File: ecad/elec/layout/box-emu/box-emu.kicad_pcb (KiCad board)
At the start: 2 copper layers, 72.5 x 63.9 mm, 70 parts

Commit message: feat(ecad): Update ecad / atopile and improve workflow
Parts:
- removed DS1: , lib:SOD-323_L1.8-W1.3-LS2.5-RD
- removed R27: 62.5mW Thick Film Resistors 50V ±100ppm/℃ ±1% 249Ω 0402 Chi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, lib:R0402
- removed U10: , Connector_PinHeader_1.00mm:PinHeader_1x02_P1.00mm_Vertical
- removed U11: , lib:GAMEBOY_COLOR_DPAD_MEMBRANE
- removed U12, U13, U14, U15: , lib:GBC_DPAD_BUTTON
- removed U16, U19: , lib:GAMEBOY_COLOR_A_B_BUTTON_MEMBRANE
- removed U17, U18, U20, U21: , lib:GBC_A_B_BUTTON
- removed U22: , lib:GAMEBOY_COLOR_START_SELECT_MEMBRANE
- removed U23, U24: , lib:GBC_START_SELECT_BUTTON
- removed U25, U26: , lib:SW-SMD_TS24CA
- removed U27: , lib:BOX_EMU
- removed U28, U29: , lib:2X06_EDGE_REVERSED
- removed U30: , lib:2X02_EDGE_REVERSED
- removed U7: , lib:DFN-8_L2.0-W2.0-P0.50-BL-EP
- removed U8: , lib:SIM-SMD_C9900007362
- removed U9: , lib:VSSOP-10_L3.0-W3.0-P0.50-LS4.9-BL
- added C10: 22µF ±20%, Samsung_Electro_Mechanics_CL21A226MAQNNNE:C0805, F.Cu at (343.7, -323.6)
- added C11: 22µF ±20%, Samsung_Electro_Mechanics_CL21A226MAQNNNE:C0805, F.Cu at (343.7, -333.6)
- added C12: 100nF ±10%, Samsung_Electro_Mechanics_CL05B104KO5NNNC:C0402, F.Cu at (343.7, -363.6)
- added C13: 100nF ±10%, Samsung_Electro_Mechanics_CL05B104KO5NNNC:C0402, F.Cu at (343.7, -373.6)
- added CN1: , JST_Sales_America_S2B_PH_SM4_TB_LF__SN:CONN-SMD_P2.00_S2B-PH-SM4-TB-LF-SN, B.Cu at (32.4, 24.6)
- added CN2: , JST_Sales_America_SM04B_SRSS_TB_LF__SN:CONN-SMD_4P-P1.00_SM04B-SRSS-TB-LF-SN, F.Cu at (73.7, -33.6)
- added D1: , Guangdong_Hottech_1N5819WS:SOD-323_L1.8-W1.3-LS2.5-RD, F.Cu at (29.6, 17.7)
- added H1: , Ckmtw_B_2100S02P_A110:HDR-TH_2P-P2.54-V-M-1, F.Cu at (44.8, -31.2)
- added J2: , PMOD_2X06_EDGE:2X06_EDGE_REVERSED, F.Cu at (310.0, 0.00)
- added J3: , PMOD_2X06_EDGE:2X06_EDGE_REVERSED, F.Cu at (320.0, 0.00)
- added MECH1: , GBC_A_B_MEMBRANE:GAMEBOY_COLOR_A_B_BUTTON_MEMBRANE, F.Cu at (64.8, -4.19)
- added MECH2: , GBC_A_B_MEMBRANE:GAMEBOY_COLOR_A_B_BUTTON_MEMBRANE, F.Cu at (59.6, -19.4)
- added MECH3: , GBC_DPAD_MEMBRANE:GAMEBOY_COLOR_DPAD_MEMBRANE, F.Cu at (20.8, -11.8)
- added MECH4: , BOX_EMU_BASE_OUTLINE:BOX_EMU_BASE, F.Cu at (43.7, -33.6)
- added MECH5: , GBC_START_SELECT_MEMBRANE:GAMEBOY_COLOR_START_SELECT_MEMBRANE, F.Cu at (42.2, 10.4)
- added MECH6: , BOX_EMU_OUTLINE:BOX_EMU, F.Cu at (300.0, 0.00)
- added SW1: , GBC_A_B_BUTTON:GBC_A_B_BUTTON, F.Cu at (71.8, -6.60)
- added SW10: , GBC_START_SELECT_BUTTON:GBC_START_SELECT_BUTTON, F.Cu at (48.4, 10.4)
- added SW11: , SHOU_HAN_TS24CA:SW-SMD_2P-TS24CA, F.Cu at (21.9, 29.1)
- added SW12: , SHOU_HAN_TS24CA:SW-SMD_2P-TS24CA, F.Cu at (27.9, 30.0)
- added SW2: , GBC_A_B_BUTTON:GBC_A_B_BUTTON, F.Cu at (57.9, -1.63)
- added SW3: , GBC_A_B_BUTTON:GBC_A_B_BUTTON, F.Cu at (66.6, -21.9)
- added SW4: , GBC_A_B_BUTTON:GBC_A_B_BUTTON, F.Cu at (52.7, -17.0)
- added SW5: , GBC_DPAD_BUTTON:GBC_DPAD_BUTTON, F.Cu at (20.8, -3.81)
- added SW6: , GBC_DPAD_BUTTON:GBC_DPAD_BUTTON, F.Cu at (12.8, -11.7)
- added SW7: , GBC_DPAD_BUTTON:GBC_DPAD_BUTTON, F.Cu at (28.8, -11.7)
- added SW8: , GBC_DPAD_BUTTON:GBC_DPAD_BUTTON, F.Cu at (20.8, -19.7)
- added SW9: , GBC_START_SELECT_BUTTON:GBC_START_SELECT_BUTTON, F.Cu at (36.8, 10.4)
- added USB1: , Yuandi_TYPE_611_T3_W:USB-C-SMD_TYPE-611-T3-W, F.Cu at (42.5, 30.3)
- C1: value 16V 100nF X7R ±10% 0402 Multilayer Ceramic Capacitors MLCC - SMD/SMT ROHS -> 100nF ±10%; footprint lib:C0402 -> Samsung_Electro_Mechanics_CL05B104KO5NNNC:C0402
- C2: value 25V 10uF X5R ±10% 0805 Multilayer Ceramic Capacitors MLCC - SMD/SMT ROHS -> 1µF ±10%; footprint lib:C0805 -> Samsung_Electro_Mechanics_CL05A105KA5NQNC:C0402
- C3, C4, C5: value 25V 10uF X5R ±10% 0805 Multilayer Ceramic Capacitors MLCC - SMD/SMT ROHS -> 100nF ±10%; footprint lib:C0805 -> Samsung_Electro_Mechanics_CL05B104KO5NNNC:C0402
- C6: value 16V 100nF X7R ±10% 0402 Multilayer Ceramic Capacitors MLCC - SMD/SMT ROHS -> 4.7µF ±10%; footprint lib:C0402 -> Samsung_Electro_Mechanics_CL05A475KP5NRNC:C0402
- C7: value 10V 4.7uF X5R ±20% 0402 Multilayer Ceramic Capacitors MLCC - SMD/SMT ROHS -> 4.7µF ±10%; footprint lib:C0402 -> Samsung_Electro_Mechanics_CL05A475KP5NRNC:C0402
- C8: value 10V 4.7uF X5R ±20% 0402 Multilayer Ceramic Capacitors MLCC - SMD/SMT ROHS -> 10µF ±10%; footprint lib:C0402 -> Samsung_Electro_Mechanics_CL21A106KAYNNNE:C0805
- C9: value 16V 100nF X7R ±10% 0402 Multilayer Ceramic Capacitors MLCC - SMD/SMT ROHS -> 10µF ±10%; footprint lib:C0402 -> Samsung_Electro_Mechanics_CL21A106KAYNNNE:C0805
- J1: footprint lib:CONN-SMD_4P-P1.00_SM04B-SRSS-TB-LF-SN -> PWR_2X02_EDGE:2X02_EDGE_REVERSED
- L1: footprint lib:IND-SMD_L2.5-W2.0_WPN252012H -> Sunlord_WPN252012H1R5MT:IND-SMD_L2.5-W2.0_WPN252012H
- LED1: footprint lib:LED0805-R-RD -> Yongyu_Photoelectric_SZYY0805R:LED0805-R-RD
- R1, R2: value 62.5mW Thick Film Resistors 50V ±100ppm/℃ ±1% 4.7kΩ 0402 Chip Resistor - Surface Mount ROHS -> 1MΩ ±1%; footprint lib:R0402 -> UNI_ROYAL_0402WGF1004TCE:R0402
- R10: value 62.5mW Thick Film Resistors 50V ±100ppm/℃ ±1% 2kΩ 0402 Chip Resistor - Surface Mount ROHS -> 10kΩ ±1%; footprint lib:R0402 -> UNI_ROYAL_0402WGF1002TCE:R0402
- R11: value 62.5mW Thick Film Resistors 50V ±100ppm/℃ ±1% 2.55kΩ 0402 Chip Resistor - Surface Mount ROHS -> 10kΩ ±1%; footprint lib:R0402 -> UNI_ROYAL_0402WGF1002TCE:R0402
- R12, R13, R14, R15, R16, R18, R19, R20, R25, R3, R4, R5, R6: value 62.5mW Thick Film Resistors 50V ±100ppm/℃ ±1% 10kΩ 0402 Chip Resistor - Surface Mount ROHS -> 10kΩ ±1%; footprint lib:R0402 -> UNI_ROYAL_0402WGF1002TCE:R0402
- R17, R23, R24: value 62.5mW Thick Film Resistors 50V ±100ppm/℃ ±1% 10kΩ 0402 Chip Resistor - Surface Mount ROHS -> 5.1kΩ ±1%; footprint lib:R0402 -> UNI_ROYAL_0402WGF5101TCE:R0402
- R21: value 62.5mW Thick Film Resistors 50V ±100ppm/℃ ±1% 10kΩ 0402 Chip Resistor - Surface Mount ROHS -> 91kΩ ±1%; footprint lib:R0402 -> YAGEO_RC0402FR_0791KL:R0402
- R22: value 62.5mW Thick Film Resistors 50V ±100ppm/℃ ±1% 10kΩ 0402 Chip Resistor - Surface Mount ROHS -> 820kΩ ±1%; footprint lib:R0402 -> FOJAN_FRC0402F8203TS:R0402
- R26: value 62.5mW Thick Film Resistors 50V ±100ppm/℃ ±1% 255Ω 0402 Chip Resistor - Surface Mount ROHS -> 10kΩ ±1%; footprint lib:R0402 -> UNI_ROYAL_0402WGF1002TCE:R0402
- R7: value 62.5mW Thick Film Resistors ±100ppm/℃ ±1% 243kΩ 0402 Chip Resistor - Surface Mount ROHS -> 2kΩ ±1%; footprint lib:R0402 -> UNI_ROYAL_0402WGF2001TCE:R0402
- R8: value 62.5mW Thick Film Resistors 50V ±100ppm/℃ ±1% 27.4kΩ 0402 Chip Resistor - Surface Mount ROHS -> 10kΩ ±1%; footprint lib:R0402 -> UNI_ROYAL_0402WGF1002TCE:R0402
- R9: value 62.5mW Thick Film Resistors 50V ±100ppm/℃ ±1% 1MΩ 0402 Chip Resistor - Surface Mount ROHS -> 10kΩ ±1%; footprint lib:R0402 -> UNI_ROYAL_0402WGF1002TCE:R0402
- U1: footprint lib:BOX_EMU_BASE -> Texas_Instruments_DRV2605LDGSR:VSSOP-10_L3.0-W3.0-P0.50-LS4.9-BL
- U2: footprint lib:CONN-SMD_P2.00_S2B-PH-SM4-TB-LF-SN -> AWINIC_AW9523BTQR:VFQFPN-24_L4.0-W4.0-P0.50-BL-EP2.8; moved to F.Cu
- U3: footprint lib:USB-C-SMD_TYPE-611-T3-W -> Maxim_Integrated_MAX17048G_T10:TDFN-8_L2.0-W2.0-P0.50-BL-EP1.2
- U4: footprint lib:VFQFPN-24_L4.0-W4.0-P0.50-BL-EP2.8 -> Microchip_Tech_MCP73831T_2ACI_OT:SOT-23-5_L3.0-W1.7-P0.95-LS2.8-BL
- U5: footprint lib:VSON-14_L4.0-W3.0-P0.50-BL-EP_TI_DSJ -> Texas_Instruments_TPS63020DSJR:VSON-14_L4.0-W3.0-P0.50-BL-EP_TI_DSJ
- U6: footprint lib:SOT-23-5_L3.0-W1.7-P0.95-LS2.8-BL -> HOAUC_HYCW118_TF09_200B:SIM-SMD_C9900007362
- moved R25 582.5 mm to (343.7, -403.6), turned to 0 degrees
- moved R26 580.2 mm to (343.7, -413.6), turned to 0 degrees
- moved R24 572.8 mm to (343.7, -393.6), turned to 0 degrees
- moved R23 542.9 mm to (343.7, -383.6), turned to 0 degrees
- moved R22 511.4 mm to (343.7, -353.6)
- moved C9 494.4 mm to (343.7, -313.6), turned to 0 degrees
- moved C8 484.6 mm to (343.7, -303.6), turned to 0 degrees
- moved R21 469.5 mm to (343.7, -343.6), turned to 0 degrees
- moved C6 455.6 mm to (343.7, -273.6), turned to 0 degrees
- moved C7 448.0 mm to (343.7, -263.6), turned to 0 degrees
- moved C5 443.0 mm to (343.7, -253.6), turned to 0 degrees
- moved R18 402.5 mm to (343.7, -243.6), turned to 0 degrees
- moved C4 399.9 mm to (343.7, -203.6), turned to 0 degrees
- moved R17 390.8 mm to (343.7, -233.6), turned to 0 degrees
- moved R16 385.9 mm to (343.7, -223.6), turned to 0 degrees
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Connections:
- net l1 renamed 1
- net l2 renamed 2
- C1 pad 1: vcc_3v3 -> battery_measurement
- C1 pad 2: box-gnd -> gnd
- C2 pad 1: vbat -> hv
- C2 pad 2: box-gnd -> gnd
- C3 pad 1: vbat -> vcc_3v3
- C3 pad 2: box-gnd -> gnd
- C4 pad 1: vcc_5v -> vcc_3v3
- C4 pad 2: box-gnd -> gnd
- C5 pad 1: vcc_5v -> vbat
- C5 pad 2: box-gnd -> gnd
- C6 pad 1: vina -> vbat
- C6 pad 2: box-gnd -> gnd
- C7 pad 2: box-gnd -> gnd
- C8 pad 2: box-gnd -> gnd
- C9 pad 2: box-gnd -> gnd
- J1 pad 1: box-gnd -> vcc_5v
- J1 pad 2: vcc_3v3 -> gnd
- J1 pad 3: sda -> gnd
- J1 pad 4: scl -> vcc_5v
- LED1 pad 1: vbus -> pos
- LED1 pad 2: cathode -> STAT
- R1 pad 1: cc1 -> battery_measurement
- R1 pad 2: box-gnd -> gnd
- R10 pad 1: prog -> vcc_3v3
- R10 pad 2: box-gnd -> right
- R11 pad 1: cathode -> vcc_3v3
- R11 pad 2: box.mcp73831-gnd -> up
- R12 pad 1: p1_3 -> EN
- R13 pad 1: en -> vcc_3v3
- R13 pad 2: vcc_3v3 -> SCL
- R14 pad 2: up -> SDA
- R15 pad 2: down -> INTN
- R16 pad 2: left -> RSTN
- R17 pad 1: vcc_3v3 -> vbus
- R17 pad 2: right -> pos
- R18 pad 1: vcc_3v3 -> nALRT
- R18 pad 2: box.io-a -> vcc_3v3
- R19 pad 2: box.io-b -> select
- R2 pad 1: cc2 -> vbat
- R2 pad 2: box-gnd -> battery_measurement
- R20 pad 2: x -> start
- R21 pad 1: vcc_3v3 -> FB
- R21 pad 2: y -> gnd
- R22 pad 1: vcc_3v3 -> vcc_5v
- R22 pad 2: start -> FB
- R23 pad 1: vcc_3v3 -> A5
- R23 pad 2: select -> gnd
- R24 pad 1: vcc_3v3 -> B5
- R24 pad 2: vol_up -> gnd
- R26 pad 1: vbat -> vcc_3v3
- R26 pad 2: battery_measurement -> vol_up
- R3 pad 1: sda -> vcc_3v3
- R3 pad 2: vcc_3v3 -> line
- R4 pad 1: scl -> vcc_3v3
- R4 pad 2: vcc_3v3 -> buttons_abxy-b-line
- R5 pad 2: rstn -> x_y_btns-a-line
- R6 pad 2: intn -> x_y_btns-b-line
- R7 pad 1: vcc_5v -> PROG
- R7 pad 2: out -> gnd
- R8 pad 1: out -> vcc_3v3
- R8 pad 2: box-gnd -> down
- R9 pad 1: pg -> vcc_3v3
- R9 pad 2: box-gnd -> left
- U2 pad 1: vbat -> start
- U2 pad 2: box-gnd -> select
- U2 pad 3: box-gnd -> 3
- U2 pad 4: box-gnd -> nALRT
- U4 pad 1: start -> STAT
- U4 pad 2: select -> gnd
- U4 pad 3: p1_2 -> vbat
- U4 pad 4: p1_3 -> vbus
- U4 pad 5: up -> PROG
- U5 pad 1: vina -> vbat
- U5 pad 12: vina -> vbat
- U5 pad 13: box-gnd -> gnd
- U5 pad 14: pg -> PG
- U5 pad 15: box-gnd -> gnd
- U5 pad 2: box-gnd -> gnd
- U5 pad 3: out -> FB
- U6 pad 1: box.mcp73831-gnd -> box.uSD.card-1
- U6 pad 2: box-gnd -> cs-line
- U6 pad 3: vbat -> MOSI
- U6 pad 4: vbus -> vcc_3v3
- U6 pad 5: prog -> SCLK
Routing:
- net box-gnd: track 462.7 -> 0.00 mm, vias 16 -> 0
- net vcc_3v3: track 170.7 -> 0.00 mm, vias 18 -> 0
- net sda: track 151.2 -> 0.00 mm, vias 7 -> 0
- net scl: track 142.5 -> 0.00 mm, vias 4 -> 0
- net miso: track 134.2 -> 0.00 mm, vias 2 -> 0
- net battery_measurement: track 127.9 -> 0.00 mm, vias 2 -> 0
- net dm: track 86.8 -> 0.00 mm, vias 2 -> 0
- net dp: track 79.5 -> 0.00 mm, vias 2 -> 0
- net box.io-b: track 77.7 -> 0.00 mm
- net sck: track 72.4 -> 0.00 mm, vias 2 -> 0
- net mosi: track 71.1 -> 0.00 mm, vias 2 -> 0
- net cs: track 70.0 -> 0.00 mm, vias 2 -> 0
- net down: track 69.4 -> 0.00 mm, vias 2 -> 0
- net vbus: track 68.5 -> 0.00 mm, vias 4 -> 0
- net y: track 63.1 -> 0.00 mm
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- removed copper zone on F.Cu, net box-gnd
- removed copper zone on B.Cu, net vcc_3v3
- removed copper zone on B.Cu, net vcc_5v
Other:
- board text removed: "A"
- board text removed: "B"
- board text removed: "DOWN"
- board text removed: "LEFT"
- board text removed: "RIGHT"
- board text removed: "SELECT"
- board text removed: "START"
- board text removed: "UP"
- board text removed: "X"
- board text removed: "Y"

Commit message: improve workflow
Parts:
- J1: moved to B.Cu
- moved J1 311.7 mm to (21.4, -43.9)
- moved J2 275.9 mm to (36.7, -37.5)
- moved J3 263.2 mm to (59.5, -37.5)
- moved MECH6 259.5 mm to (43.8, -41.2)
- moved U6 11.4 mm to (56.9, 24.5), turned to 6 degrees
- moved USB1 1.54 mm to (42.5, 28.7)
- moved CN1 0.46 mm to (32.7, 25.0), turned to 0 degrees
- turned SW11 to 170 degrees
- turned SW12 to 174 degrees
- turned SW3 to 180 degrees
- turned SW4 to 180 degrees
- turned SW5 to 90 degrees
- turned SW7 to 180 degrees
- turned SW8 to 270 degrees

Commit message: improve placement of components and robustness of scripts
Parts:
- MECH1, MECH2: value (none) -> SILKSCREENGBC_A/B
- REF**: renamed from MECH6; value (none) -> BOX_EMU
- REF**: renamed from MECH4; value (none) -> BOX_EMU_BASE
- U$1: renamed from MECH3; value (none) -> SILKSCREENGBC_D-PAD
- U$2: renamed from MECH5; value (none) -> SILKSCREENGBC_START/SELECT
- moved R24 556.2 mm to (165.6, 133.3), turned to 180 degrees
- moved R26 552.5 mm to (164.1, 108.9), turned to 180 degrees
- moved R23 547.9 mm to (165.6, 134.6), turned to 180 degrees
- moved R25 542.0 mm to (164.1, 107.7), turned to 180 degrees
- moved C13 527.9 mm to (179.4, 128.1), turned to 180 degrees
- moved C12 526.1 mm to (162.2, 130.2)
- moved R22 520.1 mm to (147.9, 128.2), turned to 180 degrees
- moved R21 509.8 mm to (147.9, 127.0), turned to 180 degrees
- moved C11 495.7 mm to (152.7, 123.8), turned to 90 degrees
- moved C9 482.7 mm to (153.5, 130.0), turned to 180 degrees
- moved C8 472.2 mm to (143.4, 124.0), turned to 90 degrees
- moved C10 447.8 mm to (154.6, 82.3), turned to 90 degrees
- moved C6 447.8 mm to (137.4, 123.8), turned to 90 degrees
- moved C7 438.2 mm to (159.8, 134.1)
- moved C5 432.6 mm to (157.0, 136.6)
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- renumbered SW4 to U2, SW2 to U2, SW1 to U2, SW3 to U2, J3 to U2, J2 to U2, SW10 to U3, SW9 to U3, J1 to U4, SW8 to U5, SW6 to U5, SW7 to U5, SW5 to U5

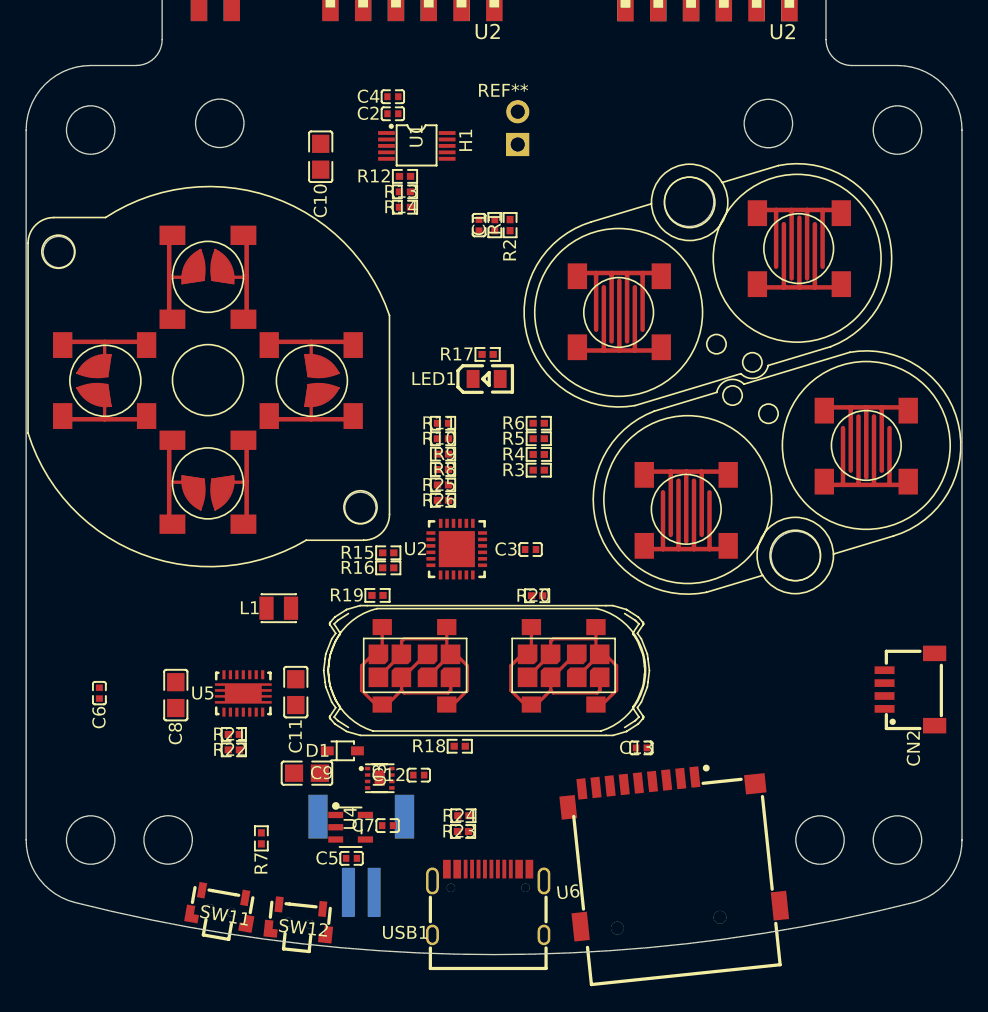
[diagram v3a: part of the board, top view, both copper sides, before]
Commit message: nudge layouts some
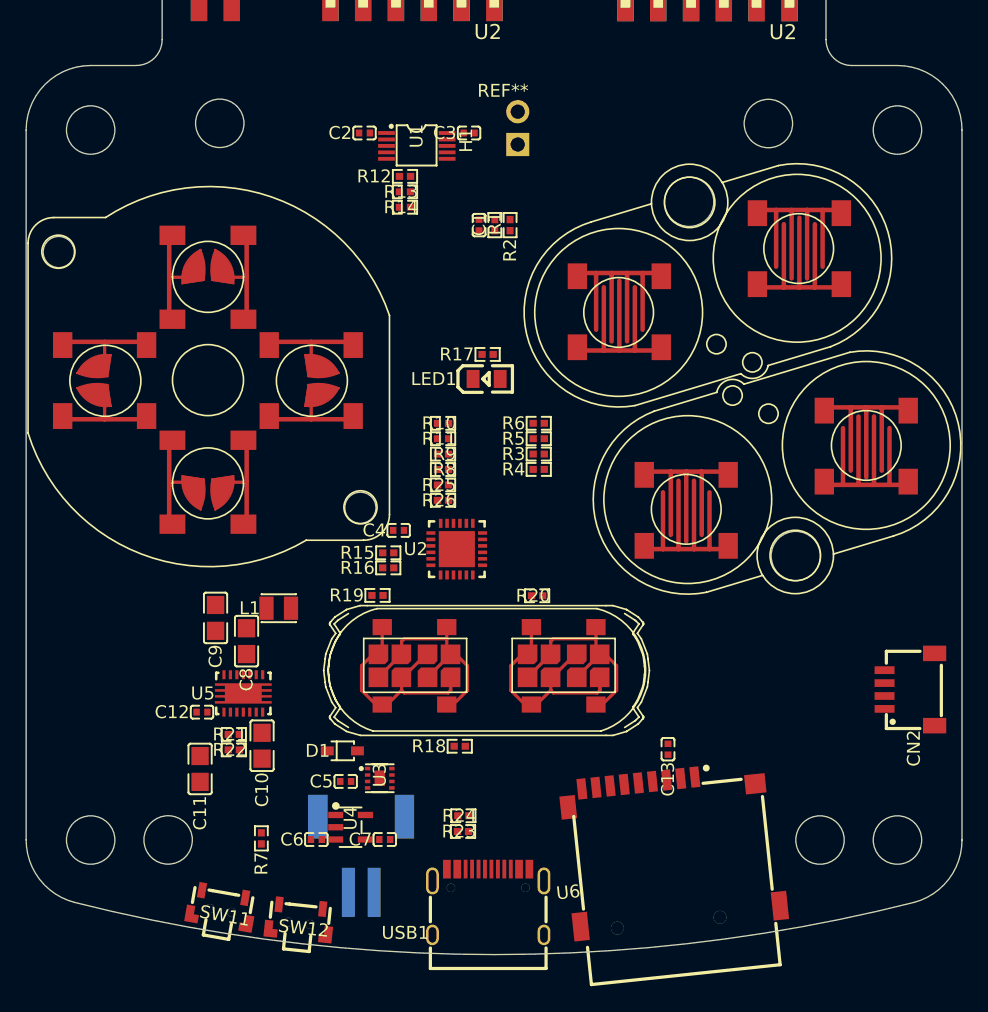
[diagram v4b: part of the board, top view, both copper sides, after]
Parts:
- moved C10 45.9 mm to (150.0, 127.9)
- moved C4 33.6 mm to (160.6, 111.2)
- moved C3 32.6 mm to (166.1, 80.4)
- moved C6 20.3 mm to (154.3, 135.2), turned to 0 degrees
- moved C12 17.5 mm to (145.4, 125.3)
- moved C9 14.0 mm to (146.4, 118.0), turned to 90 degrees
- moved C11 9.51 mm to (145.2, 129.7)
- moved C8 6.89 mm to (148.8, 119.8)
- moved C5 5.98 mm to (156.5, 130.7)
- moved C2 2.65 mm to (158.0, 80.4)
- moved C13 2.06 mm to (181.5, 128.2), turned to 90 degrees
- moved R3 1.25 mm to (171.5, 105.3)
- moved R11 1.19 mm to (164.1, 104.1)
- moved R10 1.19 mm to (164.1, 102.9)
- moved R4 1.16 mm to (171.5, 106.5)
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
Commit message: further layout changes
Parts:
- moved L1 6.66 mm to (152.2, 123.9), turned to 270 degrees
- moved C11 3.45 mm to (148.7, 129.8), turned to 180 degrees
- moved R22 2.15 mm to (146.0, 127.2)
- moved R21 2.14 mm to (146.0, 128.1), turned to 0 degrees
- moved C9 2.04 mm to (148.3, 118.9), turned to 180 degrees
- moved C10 1.36 mm to (148.7, 128.0), turned to 180 degrees
- moved C8 1.02 mm to (148.3, 120.7), turned to 180 degrees
- turned C12 to 180 degrees
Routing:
- net gnd: track 0.00 -> 21.5 mm
- net vcc_5v: track 0.00 -> 11.1 mm
- net vbat: track 0.00 -> 7.45 mm
- net FB: track 0.00 -> 5.29 mm
- net 2: track 0.00 -> 3.15 mm
- net 1: track 0.00 -> 3.15 mm

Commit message: fixing some issues
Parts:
- MECH1, MECH2: value SILKSCREENGBC_A/B -> (none)
- MECH3: renamed from REF**; value BOX_EMU_BASE -> (none)
- MECH4: renamed from REF**; value BOX_EMU -> (none)
- U$1: value SILKSCREENGBC_D-PAD -> (none)
- U$2: value SILKSCREENGBC_START/SELECT -> (none)
- renumbered U4 to J1, U2 to J2, U2 to J3, U2 to SW1, U3 to SW10, U2 to SW2, U2 to SW3, U2 to SW4, U5 to SW5, U5 to SW6, U5 to SW7, U5 to SW8, U3 to SW9
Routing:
- net gnd: track 21.5 -> 3.71 mm
- net vcc_5v: track 11.1 -> 4.03 mm
- net 2: track 3.15 -> 0.00 mm
- net 1: track 3.15 -> 0.00 mm
- net vbat: track 7.45 -> 5.69 mm, vias 0 -> 2
- added copper zone on F.Cu, net 1
- added copper zone on F.Cu, net 2
- added copper zone on F.Cu, net gnd
- added copper zone on F.Cu, net vbat
- added copper zone on F.Cu, net vcc_5v
